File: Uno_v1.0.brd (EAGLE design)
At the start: 68.6 x 53.3 mm, 64 parts, among them CN1 POWER_JACK, CN2 47346-0001, CN3 DIGITAL10, CN4 DIGITAL8, CN5 ICSP, CN6 POWER8, CN7 ANALOG6, IC1 AMS1117-5.0, IC2 AMS1117-3.3, IC3 LM358D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

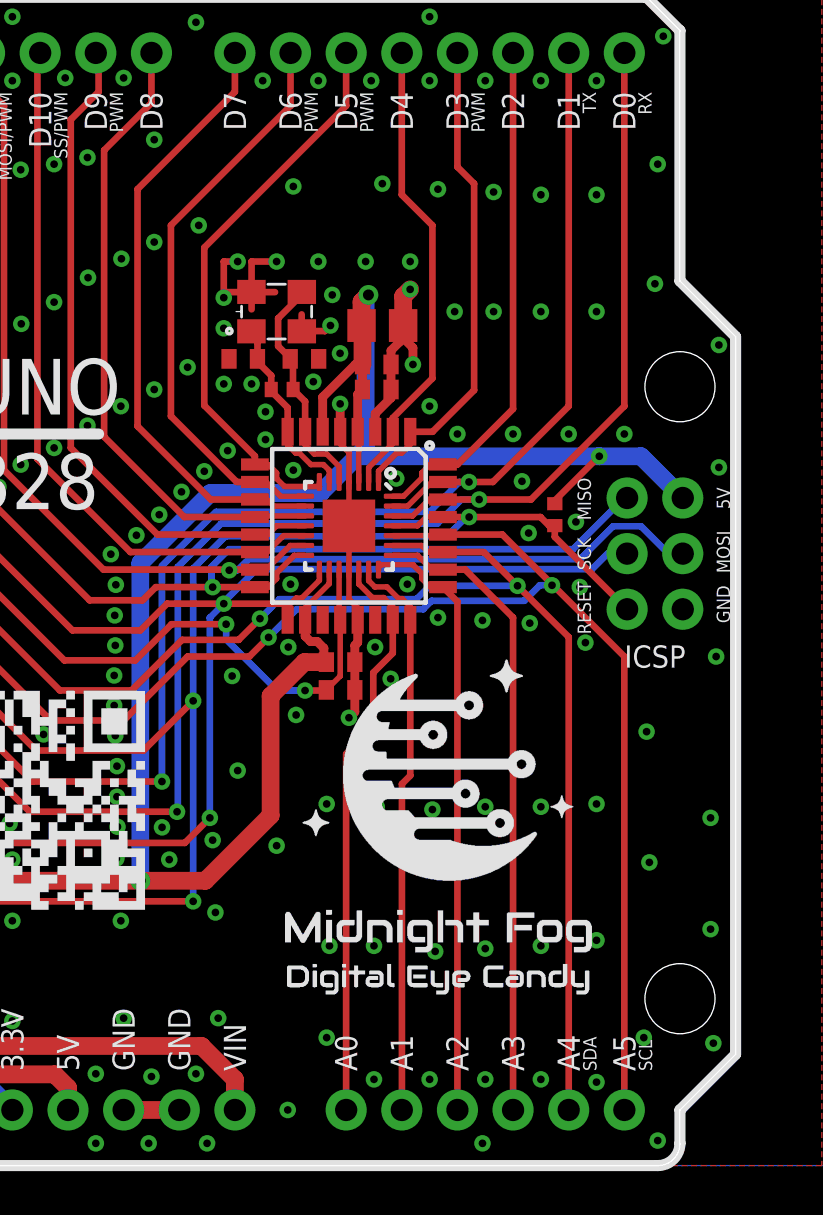
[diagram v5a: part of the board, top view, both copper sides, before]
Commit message: Moved some traces around.
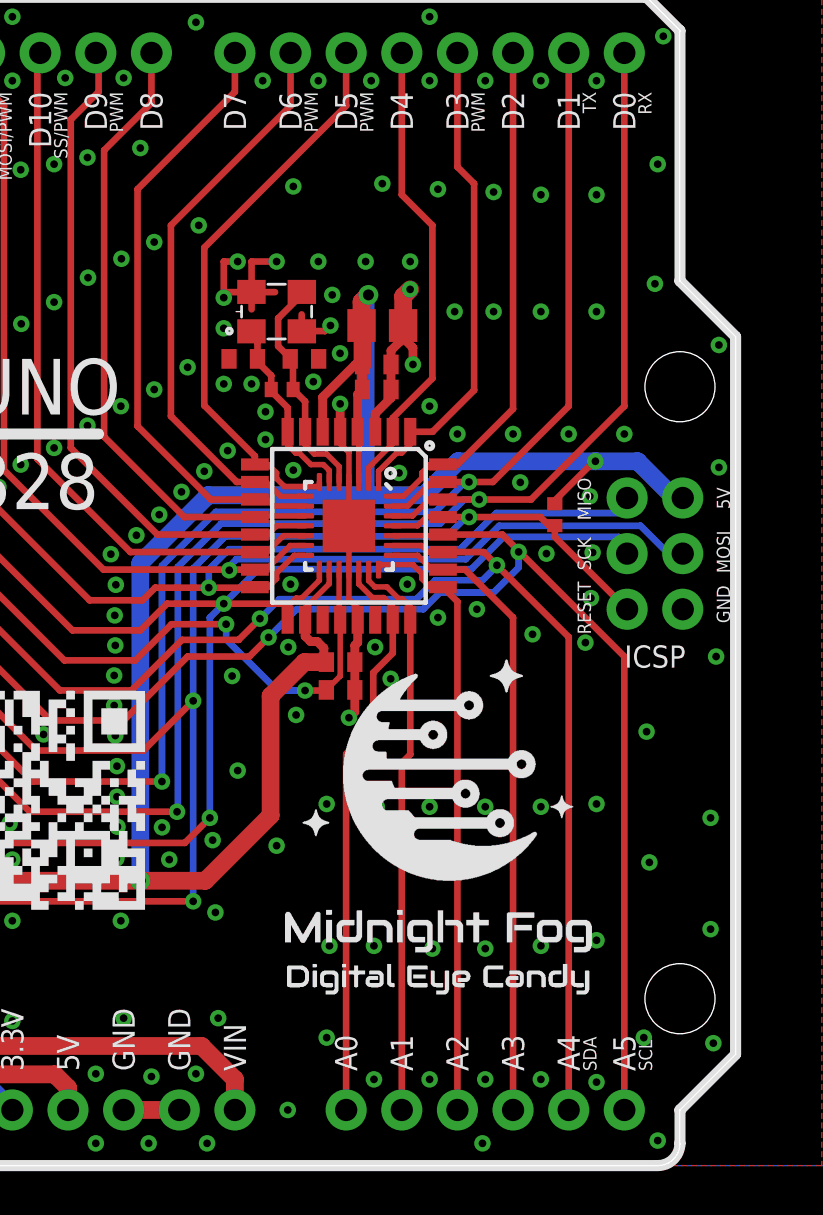
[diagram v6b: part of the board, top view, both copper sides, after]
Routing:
- net 5V: track 196.7 -> 197.8 mm
- net D13_SCK: track 111.1 -> 111.9 mm
- net A4_SDA: track 90.4 -> 89.8 mm
- net GND: vias 313 -> 314

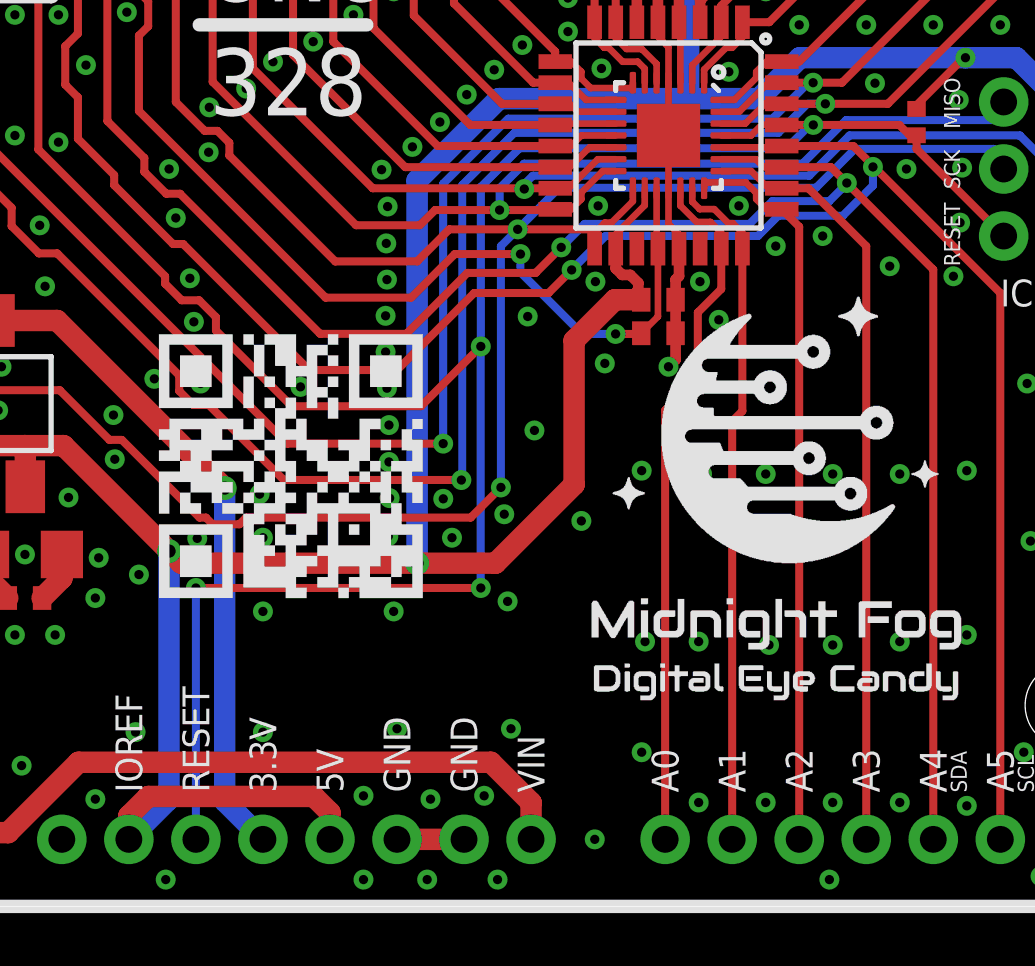
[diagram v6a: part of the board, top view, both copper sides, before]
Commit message: Moved some traces around.
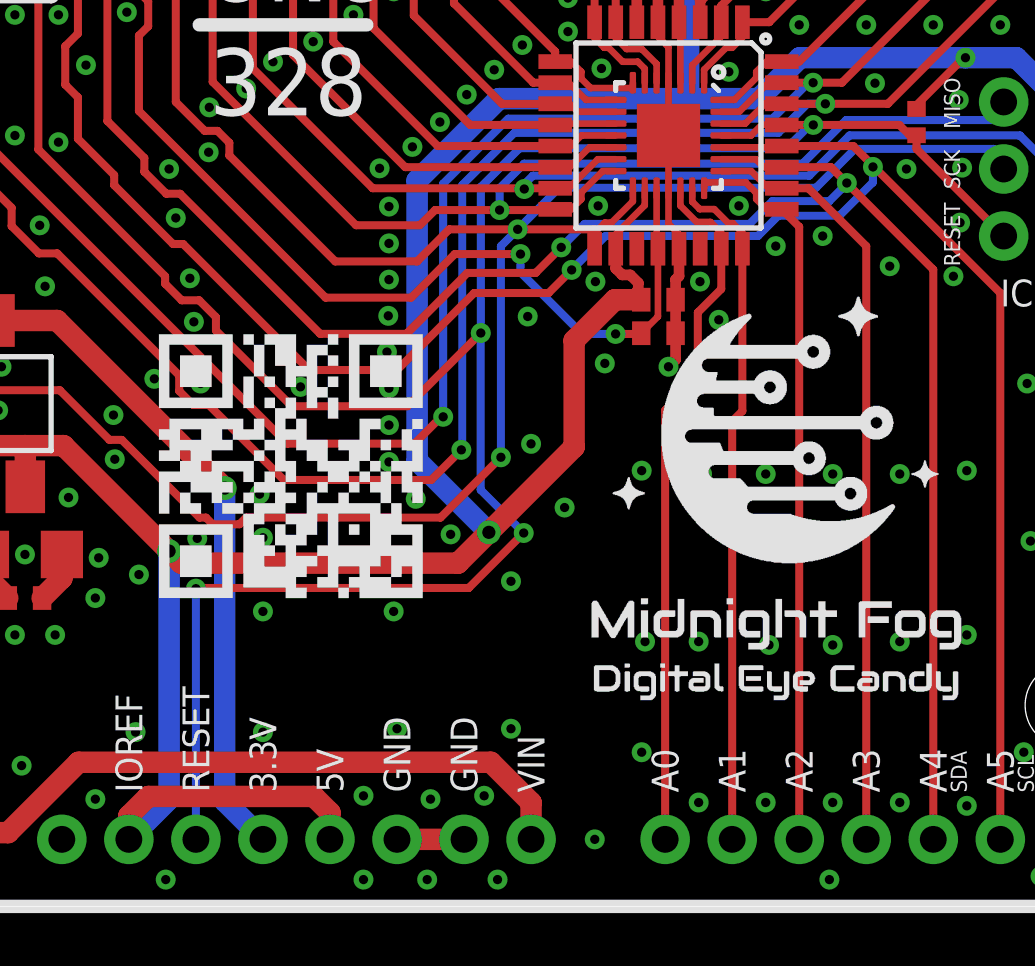
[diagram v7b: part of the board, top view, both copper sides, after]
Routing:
- net RESET: track 124.4 -> 125.6 mm
- net 5V: track 197.8 -> 196.9 mm
- net D0_RX: track 111.2 -> 110.5 mm
- net D13_SCK: track 111.9 -> 111.2 mm
- net D1_TX: track 110.0 -> 109.4 mm
- net GND: vias 314 -> 311

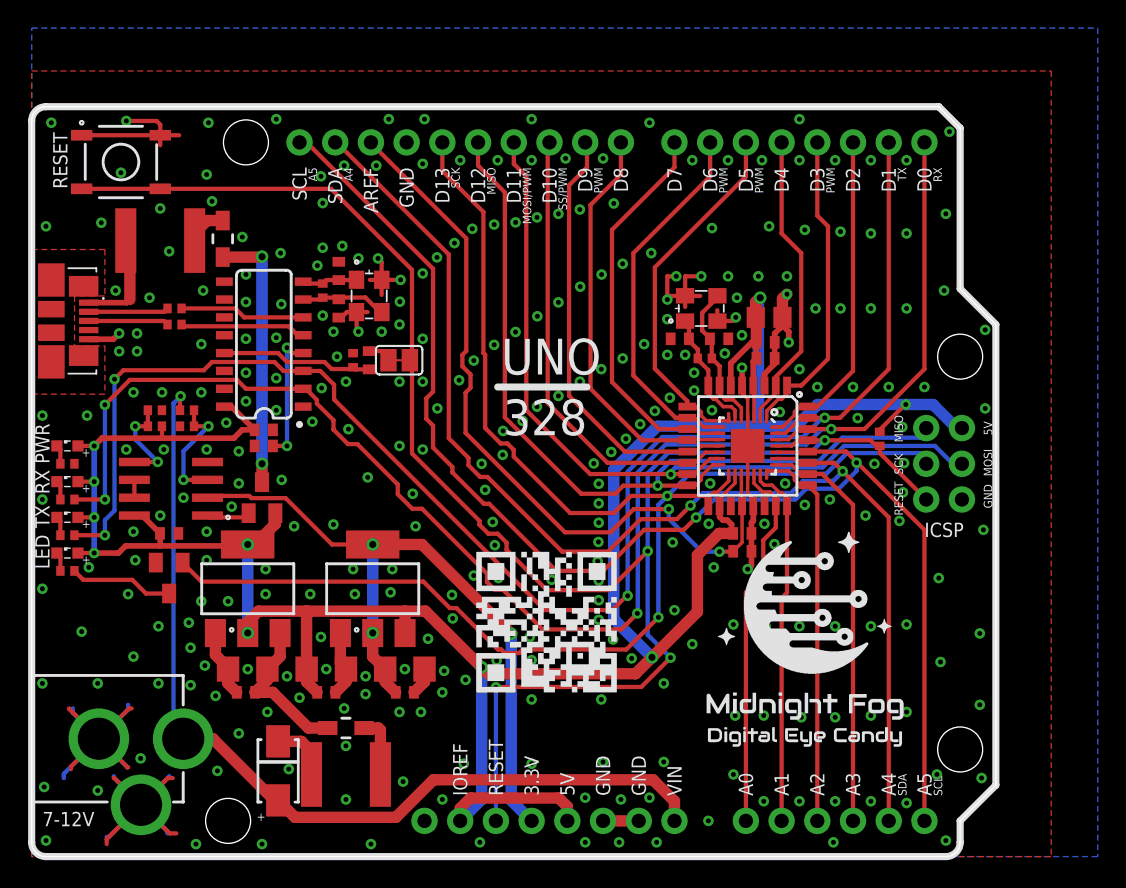
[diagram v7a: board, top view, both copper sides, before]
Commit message: Added JLCPCB tooling holes and order number placement.
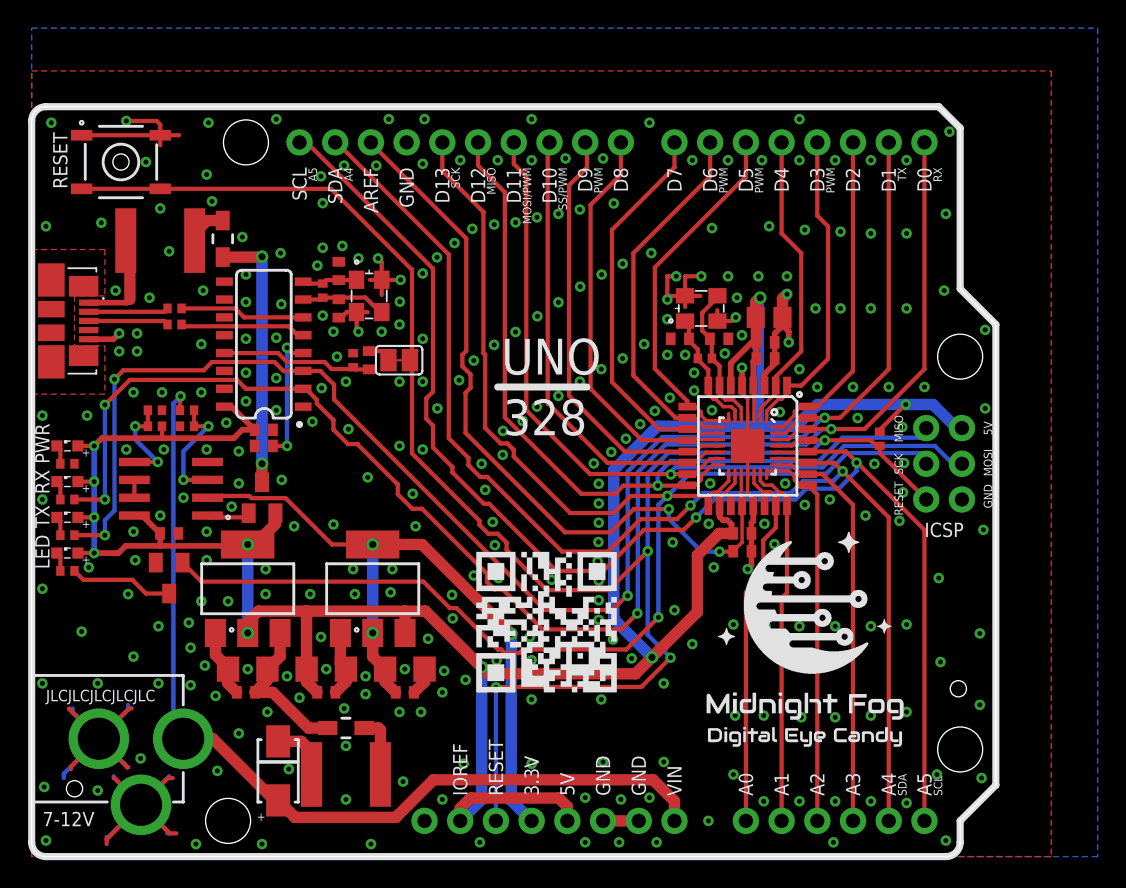
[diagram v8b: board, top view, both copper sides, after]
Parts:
- added HOLE1, HOLE2, HOLE3: TOOLINGHOLE, _my_fiducia:TOOLING-HOLE
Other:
- board text added: "JLCJLCJLCJLCJLC"
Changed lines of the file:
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@@
 <wire x1="33.147" y1="33.401" x2="39.497" y2="33.401" width="0.508" layer="21"/>
 <text x="33.528" y="29.972" size="2.54" layer="21" font="vector" ratio="16">328</text>
+<text x="1.016" y="11.049" size="0.8128" layer="21" font="vector">JLCJLCJLCJLCJLC</text>
 </plain>
 <attributes>
@@
 <attribute name="VALUE" x="5.715" y="31.369" size="0.6096" layer="27" font="vector"/>
 </element>
+<element name="HOLE1" library="_my_fiducia" package="TOOLING-HOLE" value="TOOLINGHOLE" x="6.35" y="49.403" smashed="yes"/>
+<element name="HOLE2" library="_my_fiducia" package="TOOLING-HOLE" value="TOOLINGHOLE" x="3.048" y="4.826" smashed="yes"/>
+<element name="HOLE3" library="_my_fiducia" package="TOOLING-HOLE" value="TOOLINGHOLE" x="65.913" y="11.938" smashed="yes"/>
 </elements>
 <signals>
@@
 <via x="20.701" y="46.482" extent="1-16" drill="0.35"/>
 <via x="12.446" y="48.514" extent="1-16" drill="0.35"/>
-<via x="6.35" y="48.641" extent="1-16" drill="0.35"/>
+<via x="8.128" y="49.403" extent="1-16" drill="0.35"/>
 <via x="1.397" y="52.197" extent="1-16" drill="0.35"/>
 <via x="22.352" y="4.064" extent="1-16" drill="0.35"/>
